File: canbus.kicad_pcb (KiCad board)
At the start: 2 copper layers, 15 parts, among them J1 Conn_01x08, J2 RJ45, J3 RJ45, U1 MCP2515-E/SO, U2 MCP2562-H/SN, Y1 Crystal_GND24

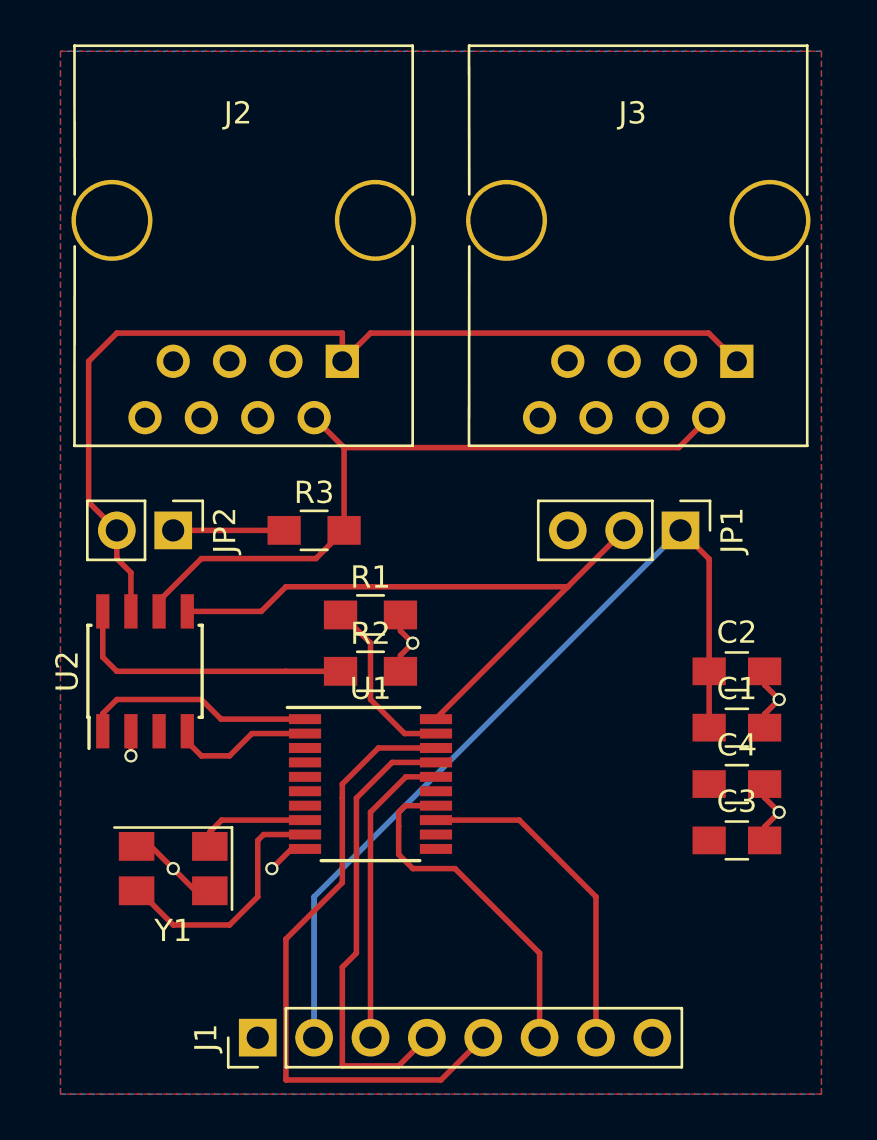
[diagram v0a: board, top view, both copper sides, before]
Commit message: I'm a fool who forgot to add edge cuts
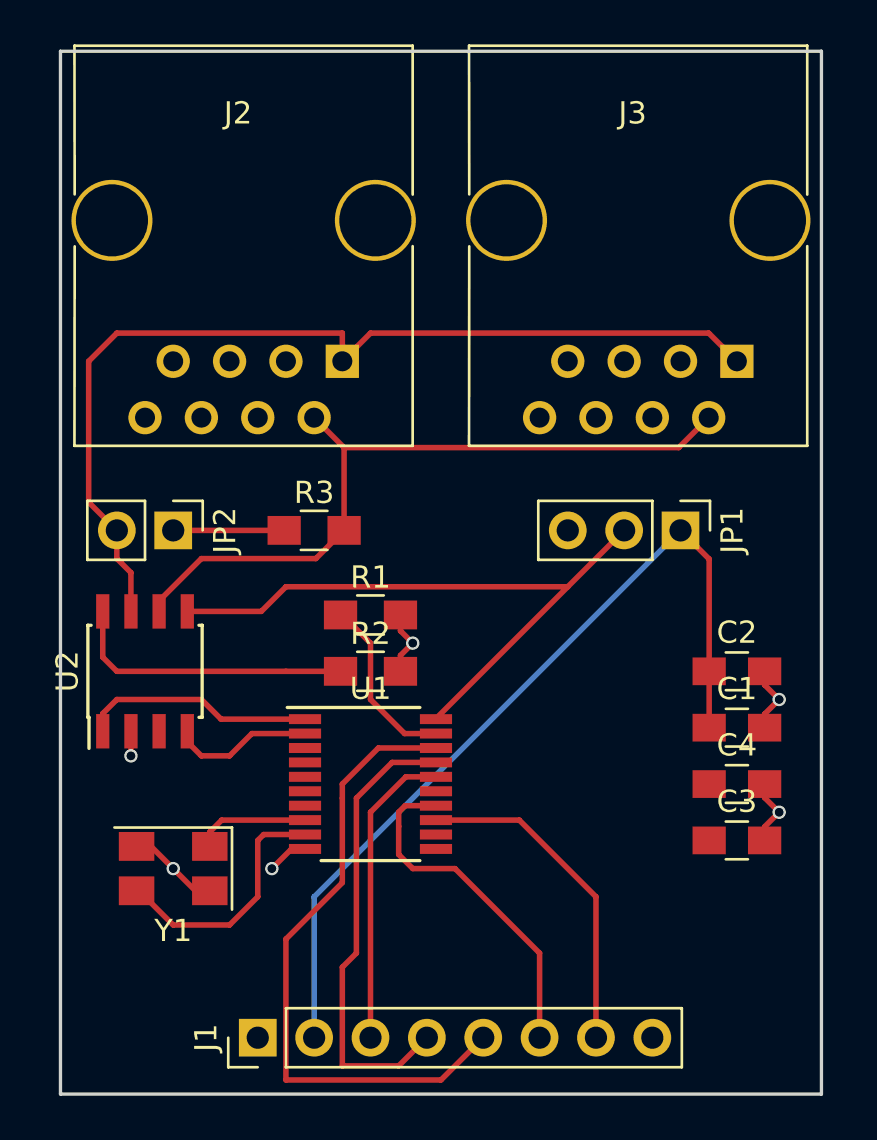
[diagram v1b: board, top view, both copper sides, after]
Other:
- board outline added: 34.3 x 47 mm
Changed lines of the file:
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@@
     (links 37)
     (no_connects 0)
-    (area 96.852381 74.454999 172.705001 137.445)
+    (area 137.665 74.204999 172.720001 124.127619)
     (thickness 1.6)
-    (drawings 0)
+    (drawings 4)
     (tracks 116)
     (zones 0)
@@
     )
   )
+  (gr_line (start 138.43 121.92) (end 138.43 74.93) (angle 90) (layer Edge.Cuts) (width 0.15))
+  (gr_line (start 172.72 121.92) (end 138.43 121.92) (angle 90) (layer Edge.Cuts) (width 0.15))
+  (gr_line (start 172.72 74.93) (end 172.72 121.92) (angle 90) (layer Edge.Cuts) (width 0.15))
+  (gr_line (start 138.43 74.93) (end 172.72 74.93) (angle 90) (layer Edge.Cuts) (width 0.15))
   (segment (start 149.86 119.38) (end 149.86 113.03) (width 0.25) (layer B.Cu) (net 1))
   (segment (start 149.86 113.03) (end 166.37 96.52) (width 0.25) (layer B.Cu) (net 1))

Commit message: Changed MCP2515 to SOIC-18 - Unfinished
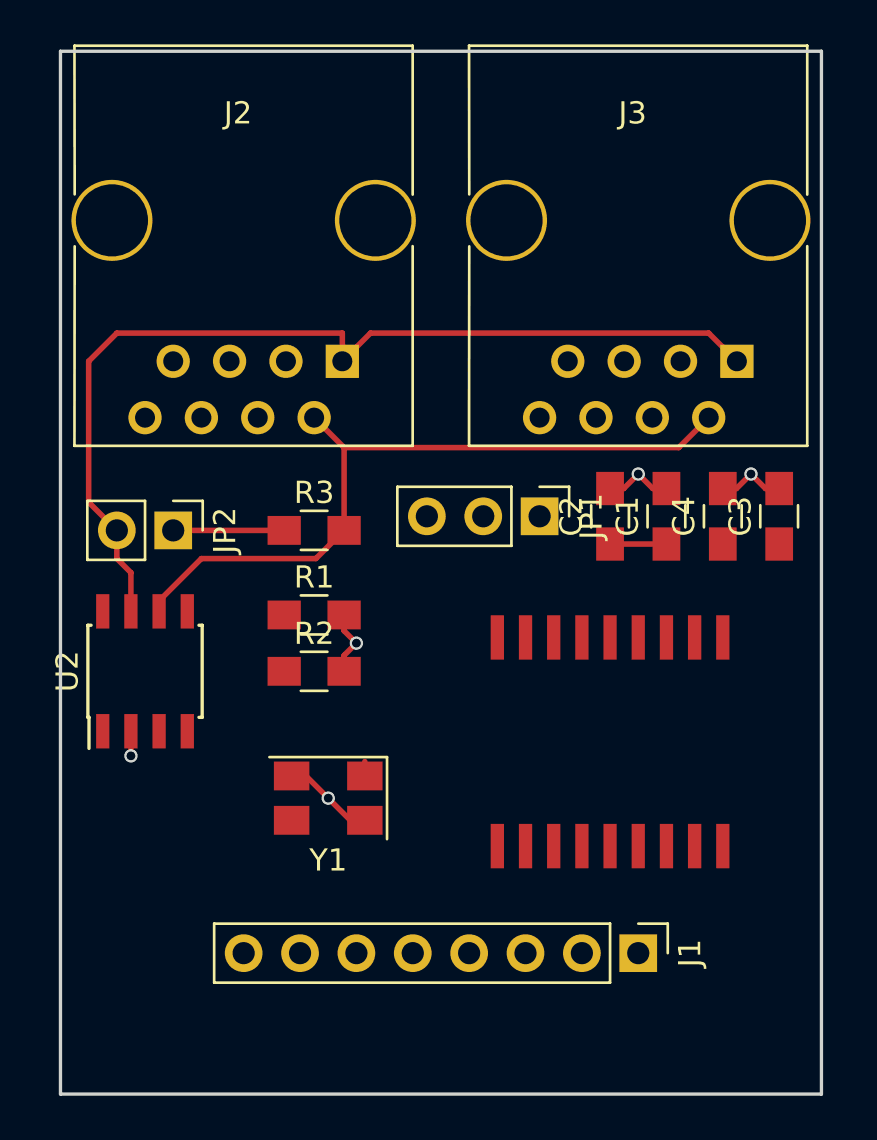
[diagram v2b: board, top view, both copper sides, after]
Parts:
- U1: footprint Housings_SSOP:TSSOP-20_4.4x6.5mm_Pitch0.65mm -> soic-18:SOIC-18
- moved J1 17.6 mm to (164.5, 115.6), turned to 270 degrees
- moved C3 14.7 mm to (170.8, 95.9), turned to 90 degrees
- moved C4 12.1 mm to (168.3, 95.9), turned to 90 degrees
- moved U1 11.0 mm to (163.2, 106.0), turned to 270 degrees
- moved C1 10.0 mm to (165.7, 95.9), turned to 90 degrees
- moved C2 9.03 mm to (163.2, 95.9), turned to 90 degrees
- moved Y1 7.67 mm to (150.5, 108.6)
- moved JP1 6.38 mm to (160.0, 95.9)
- moved R1 2.54 mm to (149.9, 100.3)
- moved R2 2.54 mm to (149.9, 102.9)
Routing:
- net +3V3: track 39.1 -> 2.54 mm
- net /VREF: track 29.6 -> 0.00 mm
- net /CS: track 29.0 -> 0.00 mm
- net /SO: track 20.9 -> 0.00 mm
- net /SCK: track 15.7 -> 0.00 mm
- net /INT: track 15.0 -> 0.00 mm
- net /SI: track 13.8 -> 0.00 mm
- net Net-(R2-Pad1): track 13.0 -> 0.00 mm
- net Net-(U1-Pad9): track 11.4 -> 0.11 mm
- net Net-(U1-Pad1): track 10.5 -> 0.00 mm
- net Net-(R1-Pad1): track 8.00 -> 0.08 mm
- net Net-(U1-Pad2): track 6.46 -> 0.48 mm
- net Net-(U1-Pad8): track 5.16 -> 0.65 mm
- net GND: track 16.7 -> 14.8 mm, vias 6 -> 5

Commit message: Finished pcb layout, slightly smaller than before
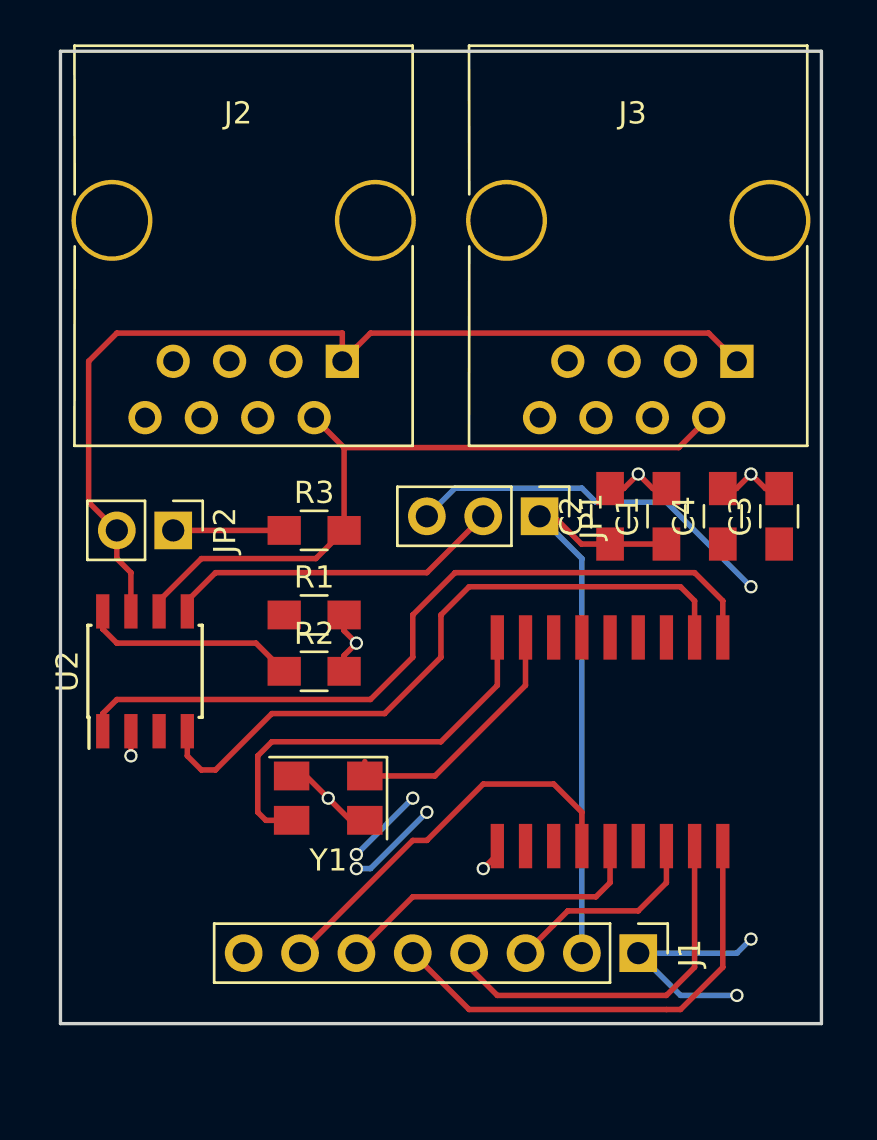
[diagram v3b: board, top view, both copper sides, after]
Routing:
- net +5V: track 0.00 -> 35.4 mm, vias 0 -> 7
- net Net-(U1-Pad1): track 0.00 -> 34.7 mm
- net Net-(U1-Pad2): track 0.48 -> 31.2 mm
- net +3V3: track 2.54 -> 26.7 mm
- net /CS: track 0.00 -> 21.3 mm
- net Net-(U1-Pad9): track 0.11 -> 18.6 mm
- net /INT: track 0.00 -> 17.9 mm
- net /SO: track 0.00 -> 17.3 mm
- net /VREF: track 0.00 -> 15.4 mm
- net /SCK: track 0.00 -> 14.4 mm
- net Net-(U1-Pad8): track 0.65 -> 11.7 mm
- net Net-(R2-Pad1): track 0.00 -> 9.76 mm
- net /SI: track 0.00 -> 9.32 mm
- net GND: track 14.8 -> 16.1 mm, vias 5 -> 6
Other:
- board size 34.3 x 47 mm -> 34.3 x 43.8 mm

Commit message: Adjusted silkscreen, shrank top edge
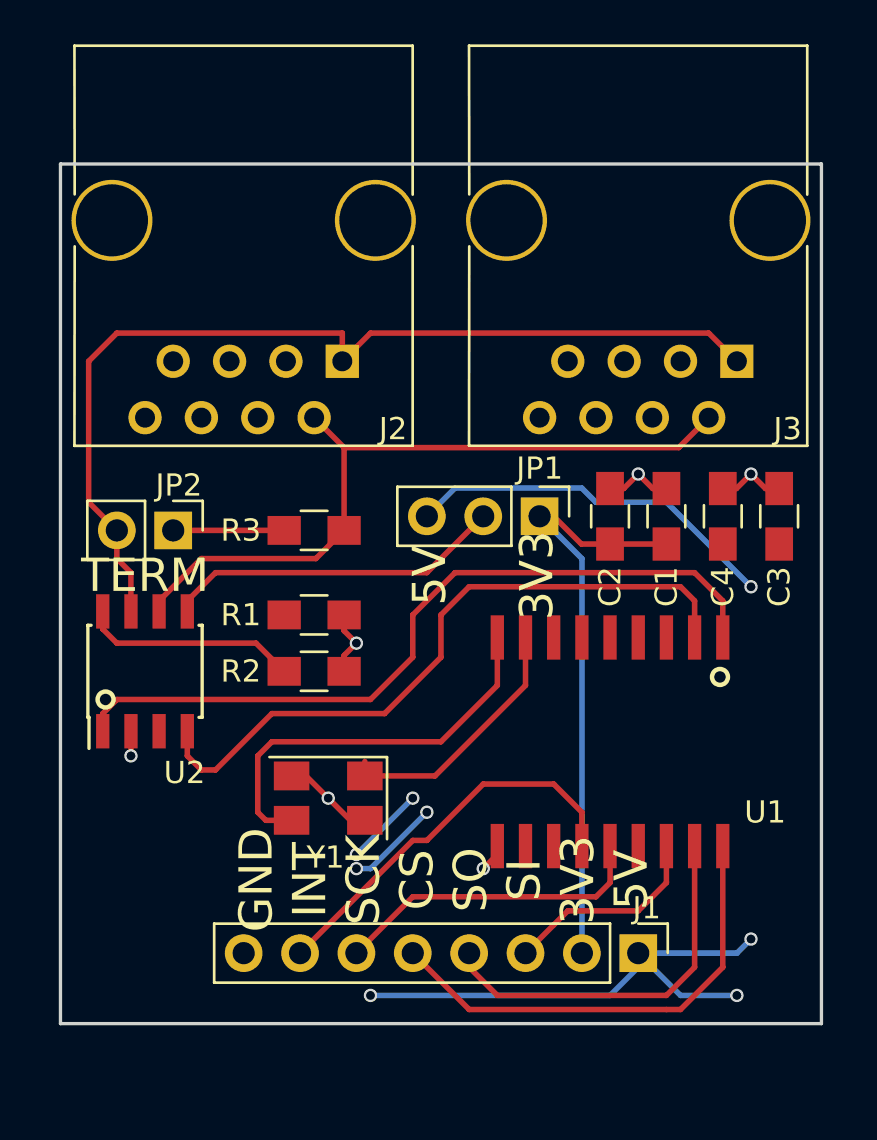
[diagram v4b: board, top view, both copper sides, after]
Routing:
- net (no net): track 0.00 -> 7.82 mm, vias 0 -> 4
- net +5V: track 35.4 -> 40.8 mm, vias 7 -> 4
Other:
- board size 34.3 x 43.8 mm -> 34.3 x 38.7 mm
- board text added: "5V 3V3"
- board text added: "GND INT SCK CS SO SI 3V3 5V"
- board text added: "TERM"
- board text added: "U1"

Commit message: Corrected schematic mistakes and updated pcb to match
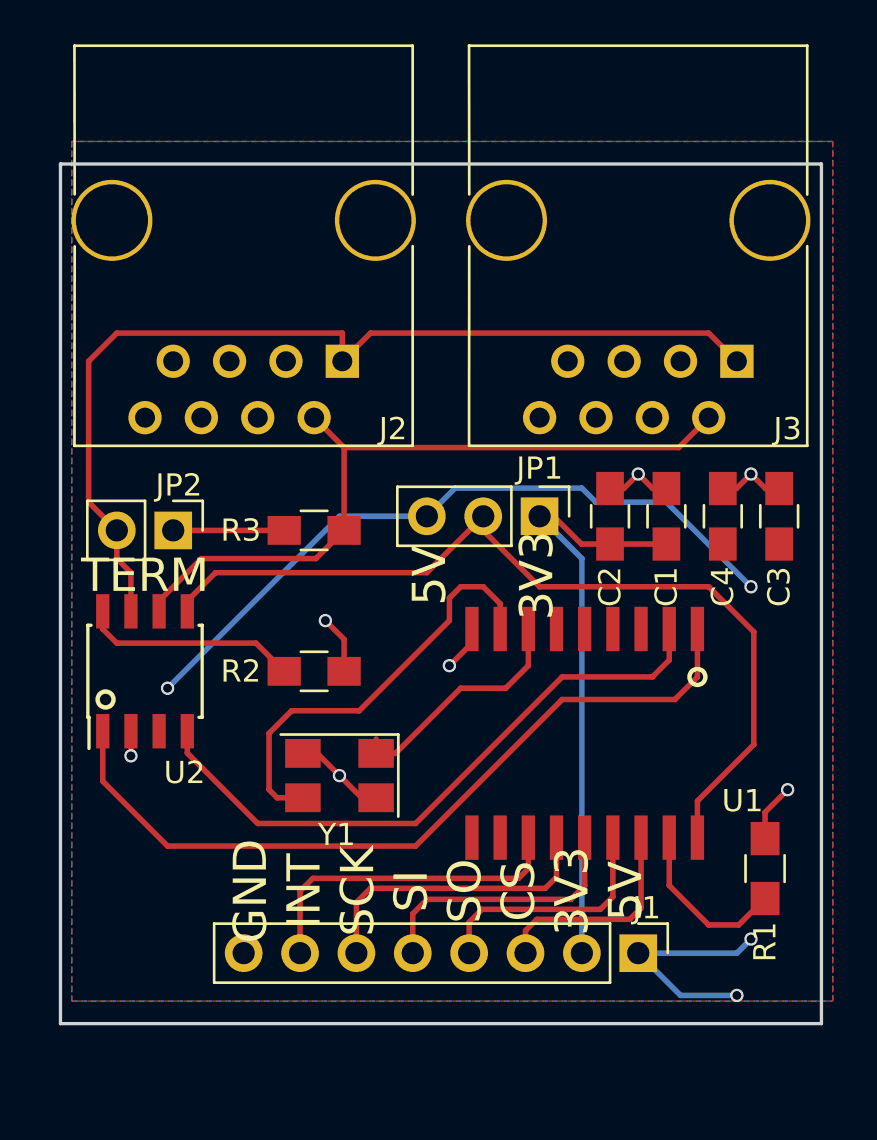
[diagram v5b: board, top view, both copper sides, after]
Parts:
- moved R1 23.3 mm to (170.2, 111.8), turned to 90 degrees
- moved U1 1.20 mm to (162.1, 105.7)
- moved Y1 1.14 mm to (151.0, 107.6)
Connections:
- J1 pad 3: /SI -> /CS
- J1 pad 5: /CS -> /SI
- U1 pad 10: GND -> Net-(U1-Pad10)
- U1 pad 12: Net-(U1-Pad12) -> /INT
- U1 pad 13: /INT -> /SCK
- U1 pad 14: /SCK -> /SI
- U1 pad 15: Net-(U1-Pad15) -> /SO
- U1 pad 16: /SI -> /CS
- U1 pad 17: /SO -> Net-(R1-Pad1)
- U1 pad 18: /CS -> /VREF
- U1 pad 9: Net-(U1-Pad9) -> GND
- Y1 pad 1: Net-(U1-Pad8) -> Net-(U1-Pad7)
- Y1 pad 3: Net-(U1-Pad9) -> Net-(U1-Pad8)
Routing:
- net /VREF: track 15.4 -> 40.4 mm
- net Net-(U1-Pad9): track 18.6 -> 0.00 mm
- net /CS: track 21.3 -> 9.82 mm
- net Net-(U1-Pad7): track 0.00 -> 10.8 mm
- net (no net): track 7.82 -> 0.00 mm, vias 4 -> 0
- net Net-(U1-Pad8): track 11.7 -> 19.5 mm
- net Net-(R1-Pad1): track 0.08 -> 7.71 mm
- net /SO: track 17.3 -> 11.6 mm
- net /INT: track 17.9 -> 14.9 mm
- net GND: track 16.1 -> 19.1 mm, vias 6 -> 7
- net /SI: track 9.32 -> 12.2 mm
- net Net-(U1-Pad2): track 31.2 -> 28.5 mm
- net +5V: track 40.8 -> 43.1 mm
- net Net-(U1-Pad1): track 34.7 -> 35.6 mm
- net /SCK: track 14.4 -> 13.6 mm
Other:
- board text added: "GND INT SCK SI SO CS 3V3 5V"
- board text removed: "GND INT SCK CS SO SI 3V3 5V"

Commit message: Flipped main connector to bottom of PCB
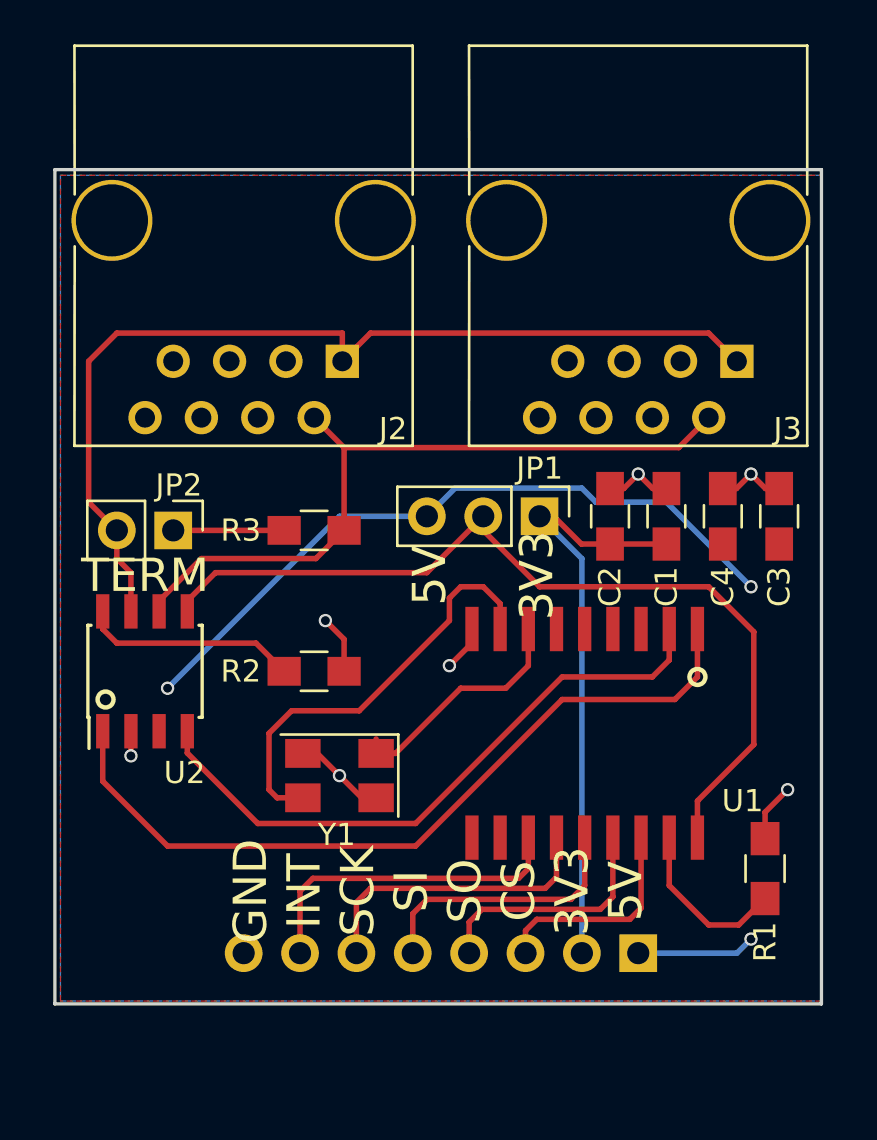
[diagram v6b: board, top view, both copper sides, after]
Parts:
- J1: moved to B.Cu
- turned J1 to 90 degrees
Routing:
- net +5V: track 43.1 -> 37.8 mm, vias 4 -> 3
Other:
- board size 34.3 x 38.7 mm -> 34.5 x 37.6 mm

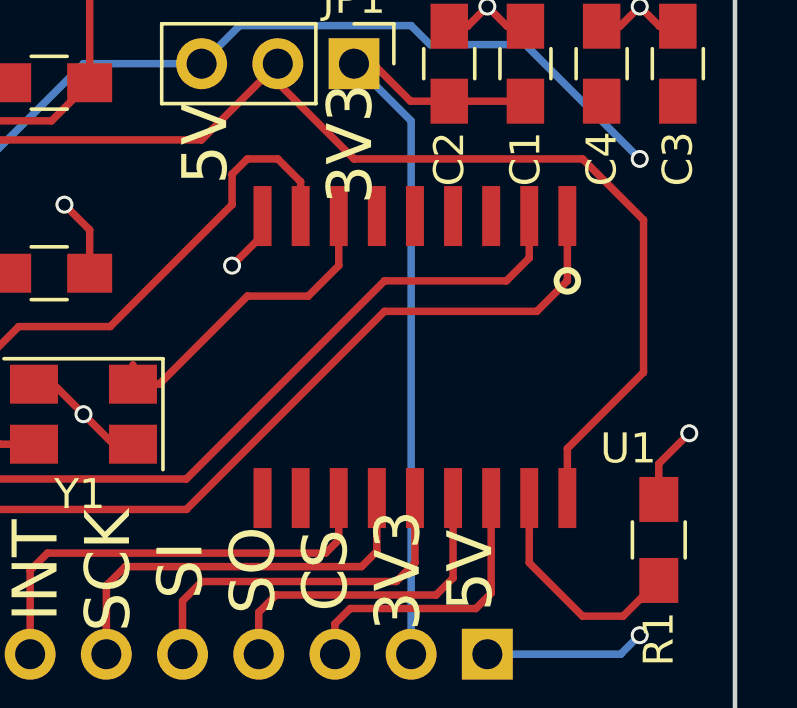
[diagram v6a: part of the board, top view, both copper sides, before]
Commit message: Changed SOIC18 footprint to builtin
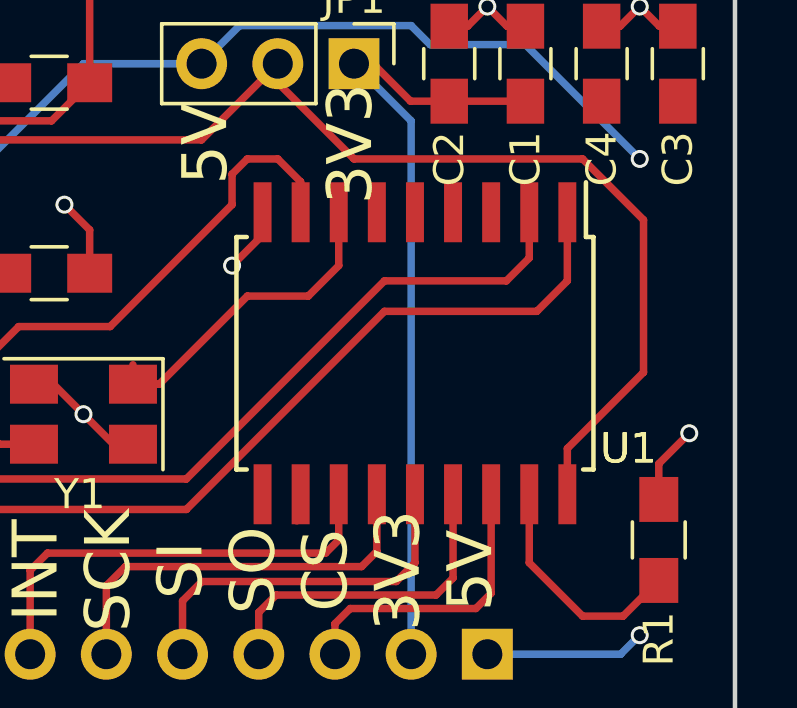
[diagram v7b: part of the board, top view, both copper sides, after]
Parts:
- U1: footprint soic-18:SOIC-18 -> Housings_SOIC:SOIC-18W_7.5x11.6mm_Pitch1.27mm
- moved U1 0.13 mm to (162.1, 105.5)
